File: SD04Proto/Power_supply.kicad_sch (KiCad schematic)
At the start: 9 parts, among them IC4 NCP730ASNADJT1G, U1 UA78M33CDCYR

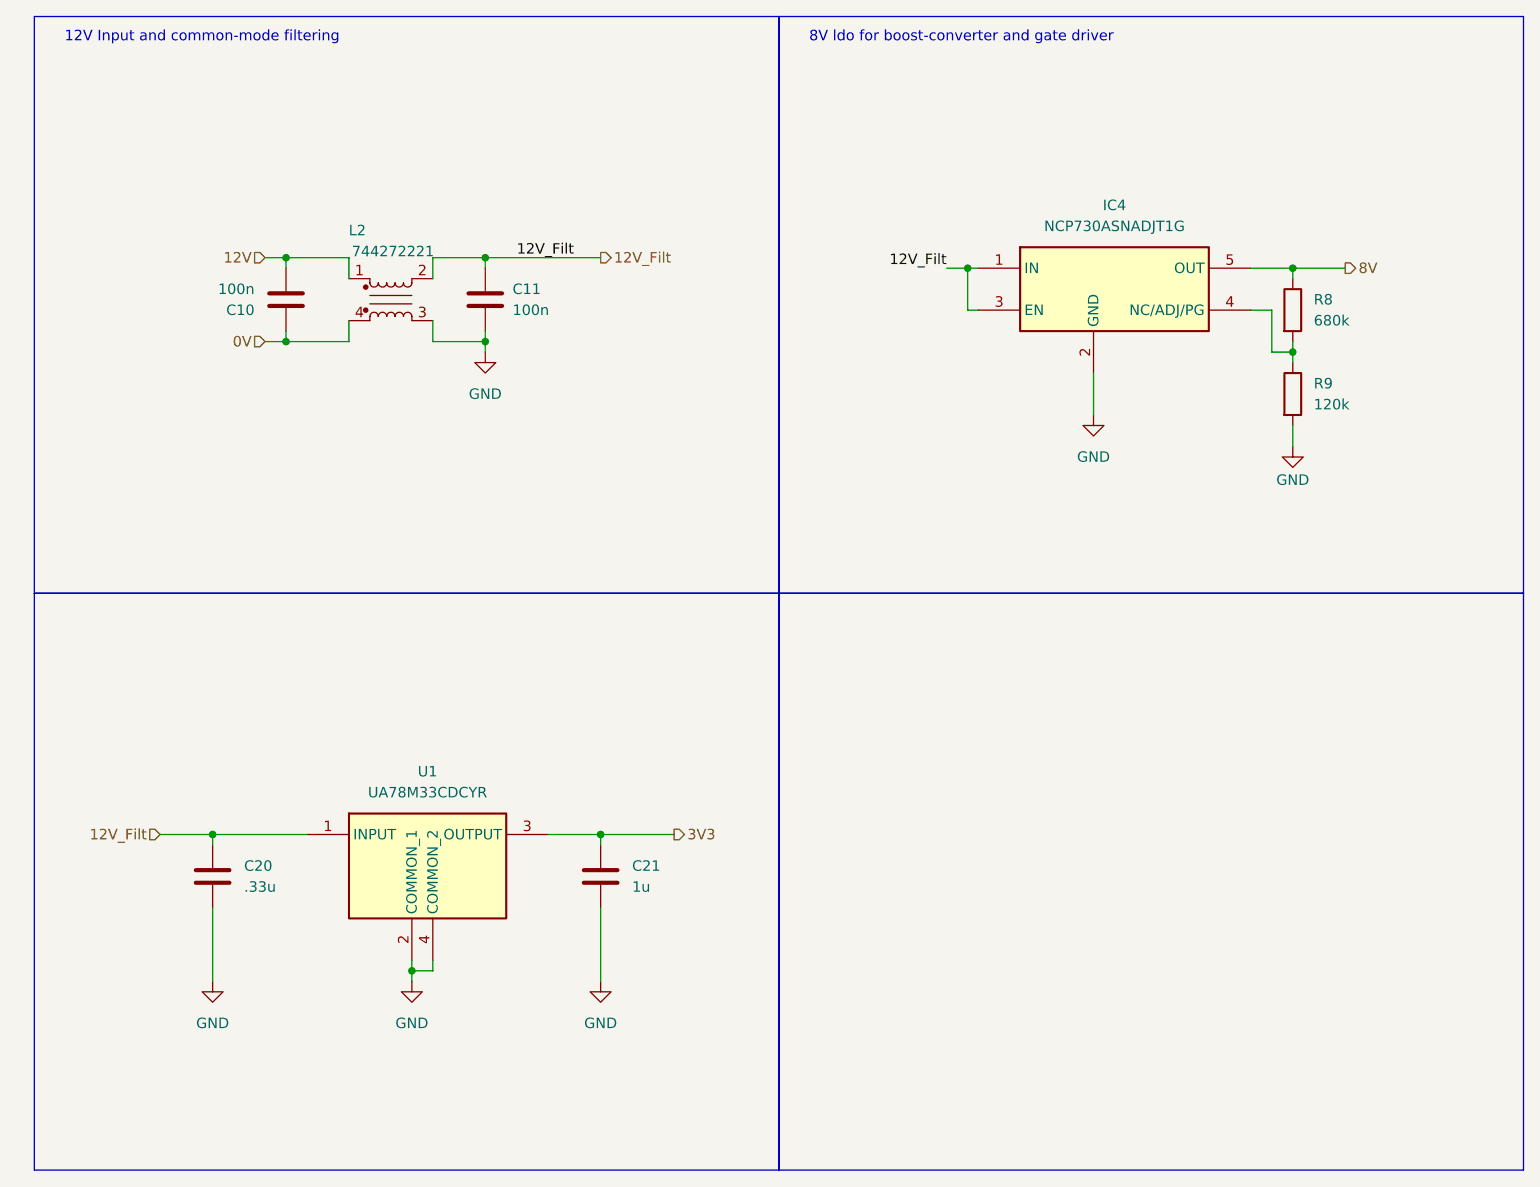
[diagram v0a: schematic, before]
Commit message: updated layout after review
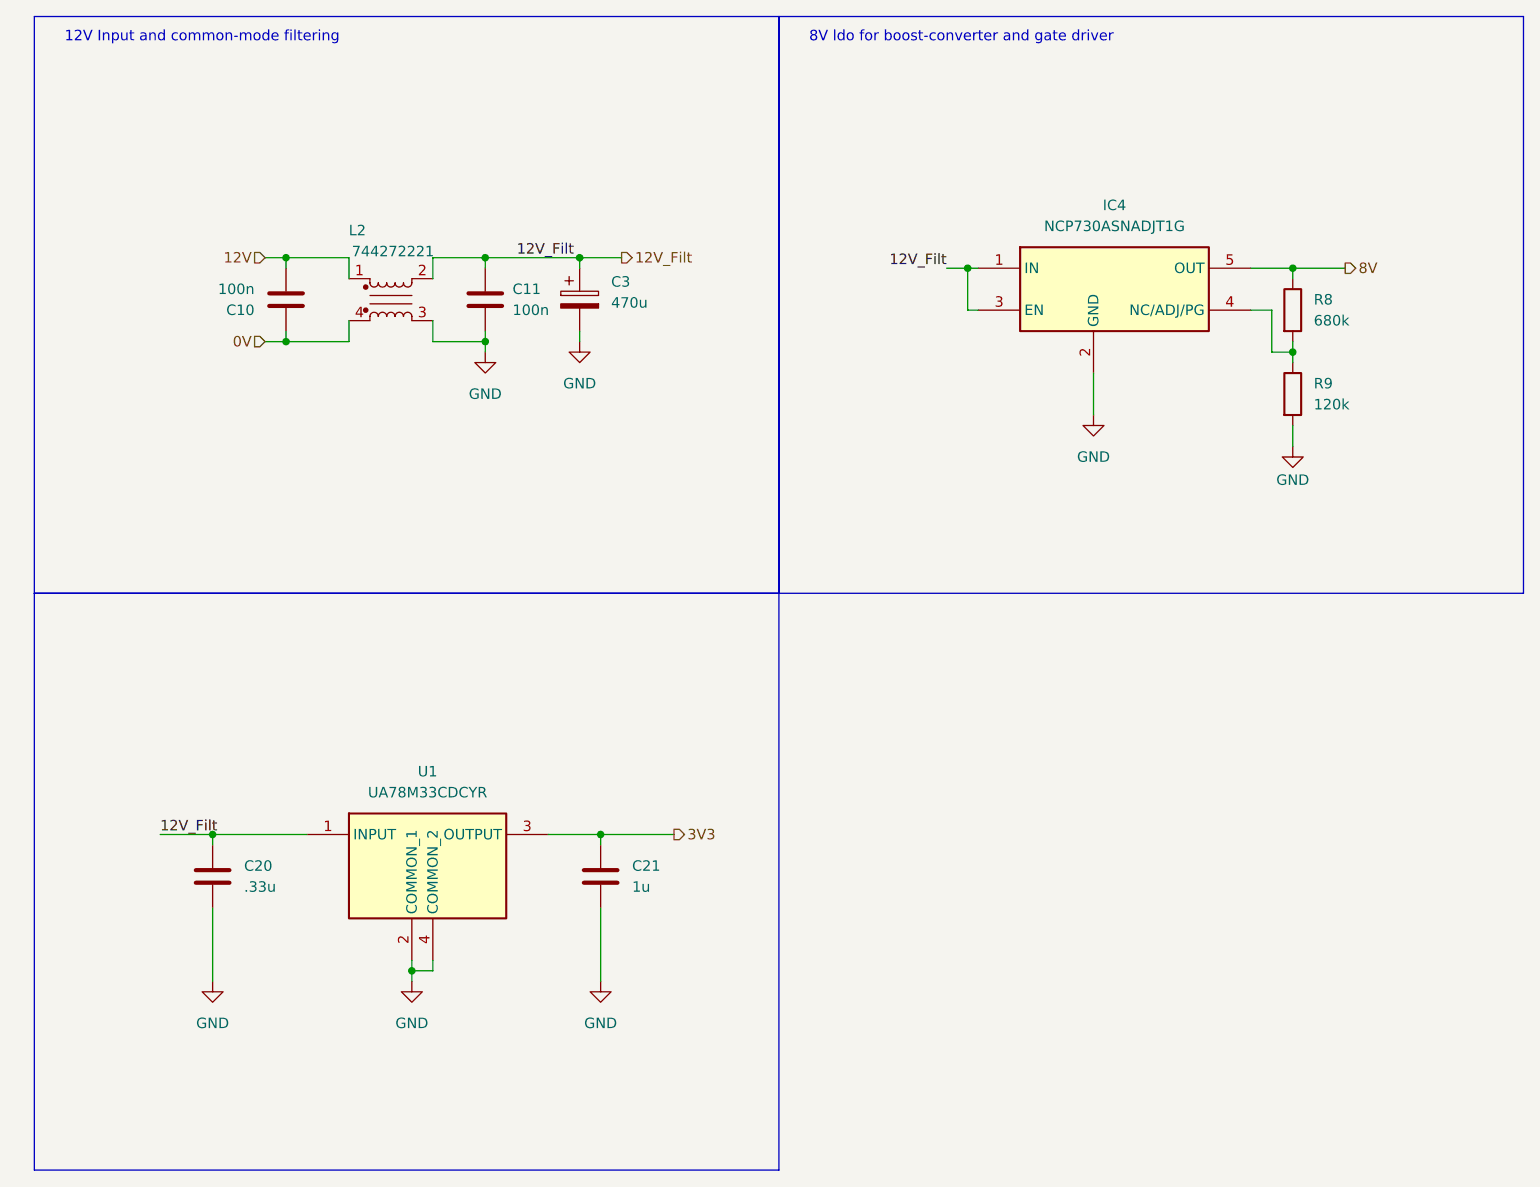
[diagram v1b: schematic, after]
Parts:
- added C3: 470u, Capacitor_SMD:CP_Elec_10x10, symbol Device:C_Polarized
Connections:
- net 12V_Filt: now also C3.1
- net GND: now also C3.2
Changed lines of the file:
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@@
-	)
-	(rectangle
-		(start 106.68 85.09)
-		(end 196.85 154.94)
-		(stroke
-			(width 0)
-			(type default)
-		)
-		(fill
-			(type none)
-		)
 	)
 	(rectangle
@@
 	)
 	(junction
+		(at 82.55 44.45)
+		(diameter 0)
+		(color 0 0 0 0)
+	)
+	(junction
 		(at 62.23 130.81)
 		(diameter 0)
@@
 	(wire
 		(pts
+			(xy 82.55 44.45) (xy 87.63 44.45)
+		)
+		(stroke
+			(width 0)
+			(type default)
+		)
+	)
+	(wire
+		(pts
 			(xy 166.37 50.8) (xy 166.37 55.88)
 		)
@@
 	(wire
 		(pts
-			(xy 71.12 44.45) (xy 85.09 44.45)
+			(xy 71.12 44.45) (xy 82.55 44.45)
 		)
 		(stroke
@@
 	(wire
 		(pts
+			(xy 82.55 53.34) (xy 82.55 54.61)
+		)
+		(stroke
+			(width 0)
+			(type default)
+		)
+	)
+	(wire
+		(pts
 			(xy 168.91 64.77) (xy 168.91 67.31)
 		)
@@
 			(width 0)
 			(type default)
+		)
+	)
+	(wire
+		(pts
+			(xy 82.55 44.45) (xy 82.55 45.72)
+		)
+		(stroke
+			(width 0)
+			(type default)
+		)
+	)
+	(label "12V_Filt"
+		(at 31.75 114.3 0)
+		(effects
+			(font
+				(size 1.27 1.27)
+			)
+			(justify left bottom)
 		)
 	)
@@
 	)
 	(hierarchical_label "12V_Filt"
-		(shape input)
-		(at 31.75 114.3 180)
-		(effects
-			(font
-				(size 1.27 1.27)
-			)
-			(justify right)
-		)
-	)
-	(hierarchical_label "12V_Filt"
 		(shape output)
-		(at 85.09 44.45 0)
+		(at 87.63 44.45 0)
 		(effects
 			(font
@@
 	)
 	(symbol
+		(lib_id "Device:C_Polarized")
+		(at 82.55 49.53 0)
+		(unit 1)
+		(exclude_from_sim no)
+		(in_bom yes)
+		(on_board yes)
+		(dnp no)
+		(fields_autoplaced yes)
+		(property "Reference" "C3"
+			(at 86.36 47.3709 0)
+			(effects
+				(font
+					(size 1.27 1.27)
+				)
+				(justify left)
+			)
+		)
+		(property "Value" "470u"
+			(at 86.36 49.9109 0)
+			(effects
+				(font
+					(size 1.27 1.27)
+				)
+				(justify left)
+			)
+		)
+		(property "Footprint" "Capacitor_SMD:CP_Elec_10x10"
+			(at 83.5152 53.34 0)
+			(effects
+				(font
+					(size 1.27 1.27)
+				)
+				(hide yes)
+			)
+		)
+		(property "Datasheet" "~"
+			(at 82.55 49.53 0)
+			(effects
+				(font
+					(size 1.27 1.27)
+				)
+				(hide yes)
+			)
+		)
+		(property "Description" "Polarized capacitor"
+			(at 82.55 49.53 0)
+			(effects
+				(font
+					(size 1.27 1.27)
+				)
+				(hide yes)
+			)
+		)
+		(pin "1"
+		)
+		(pin "2"
+		)
+		(instances
+			(project ""
+				(path "/7f4db626-1185-4eb3-a5a5-b6392b261527/6b17cb66-2f8c-4c19-8bb7-d51a84820f19"
+					(reference "C3")
+					(unit 1)
+				)
+			)
+		)
+	)
+	(symbol
 		(lib_id "power:GND")
 		(at 38.1 132.08 0)
@@
 					(unit 1)
 				)
+			)
+		)
+	)
+	(symbol
+		(lib_id "power:GND")
+		(at 82.55 54.61 0)
+		(unit 1)
+		(exclude_from_sim no)
+		(in_bom yes)
+		(on_board yes)
+		(dnp no)
+		(fields_autoplaced yes)
+		(property "Reference" "#PWR03"
+			(at 82.55 60.96 0)
+			(effects
+				(font
+					(size 1.27 1.27)
+				)
+				(hide yes)
+			)
+		)
+		(property "Value" "GND"
+			(at 82.55 59.69 0)
+			(effects
+				(font
+					(size 1.27 1.27)
+				)
+			)
+		)
+		(property "Footprint" ""
+			(at 82.55 54.61 0)
+			(effects
+				(font
+					(size 1.27 1.27)
+				)
+				(hide yes)
+			)
+		)
+		(property "Datasheet" ""
+			(at 82.55 54.61 0)
+			(effects
+				(font
+					(size 1.27 1.27)
+				)
+				(hide yes)
+			)
+		)
+		(property "Description" "Power symbol creates a global label with name \"GND\" , ground"
+			(at 82.55 54.61 0)
+			(effects
+				(font
+					(size 1.27 1.27)
+				)
+				(hide yes)
+			)
+		)
+		(pin "1"
+		)
+		(instances
+			(project ""
+				(path "/7f4db626-1185-4eb3-a5a5-b6392b261527/6b17cb66-2f8c-4c19-8bb7-d51a84820f19"
+					(reference "#PWR03")
+					(unit 1)
+				)
